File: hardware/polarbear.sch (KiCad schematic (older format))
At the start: 84 parts, among them IC1 ATMEGA32U4, J1 USBMICRO, X1 ATS16B

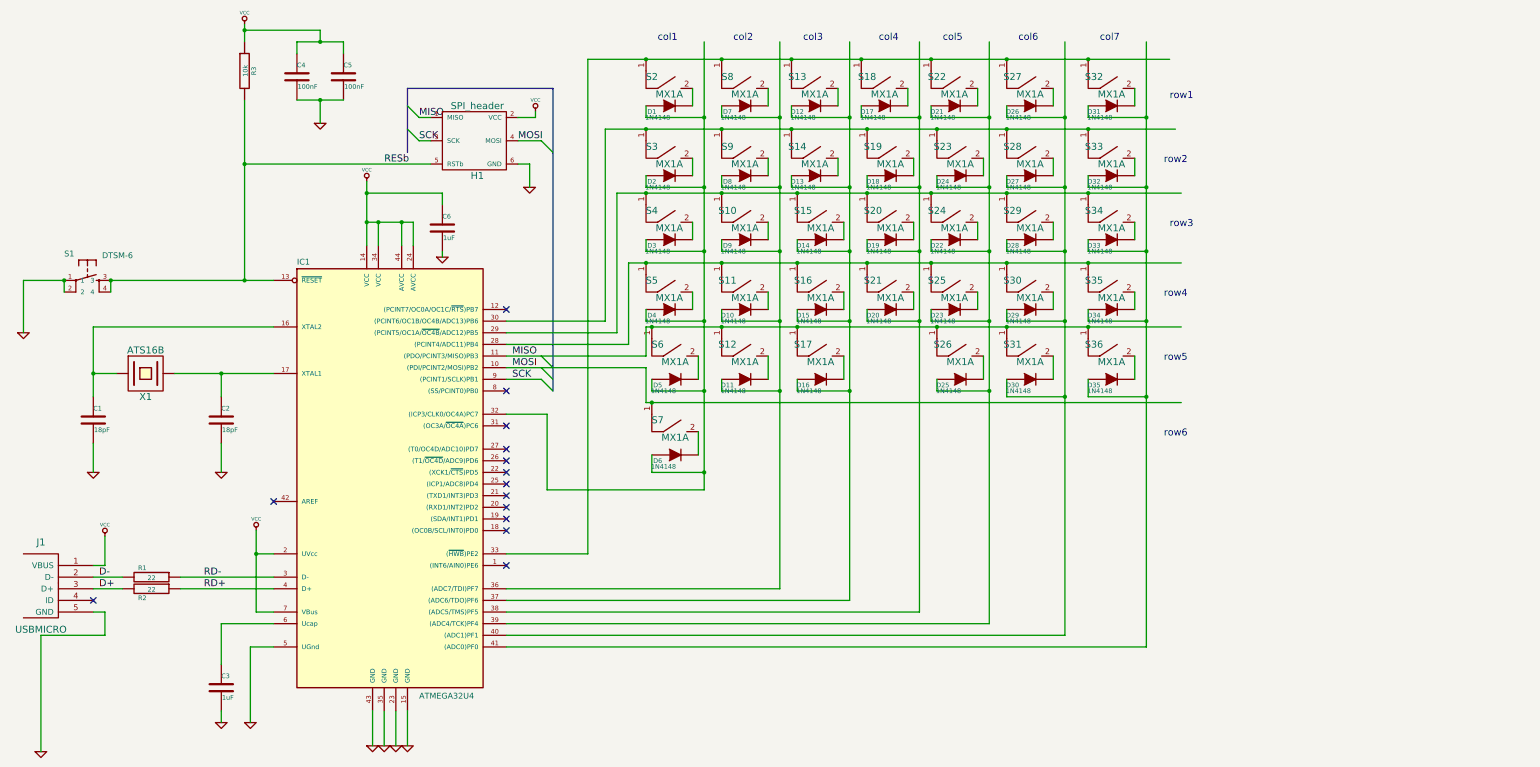
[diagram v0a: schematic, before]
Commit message: Adding support for Tennsy 2.0
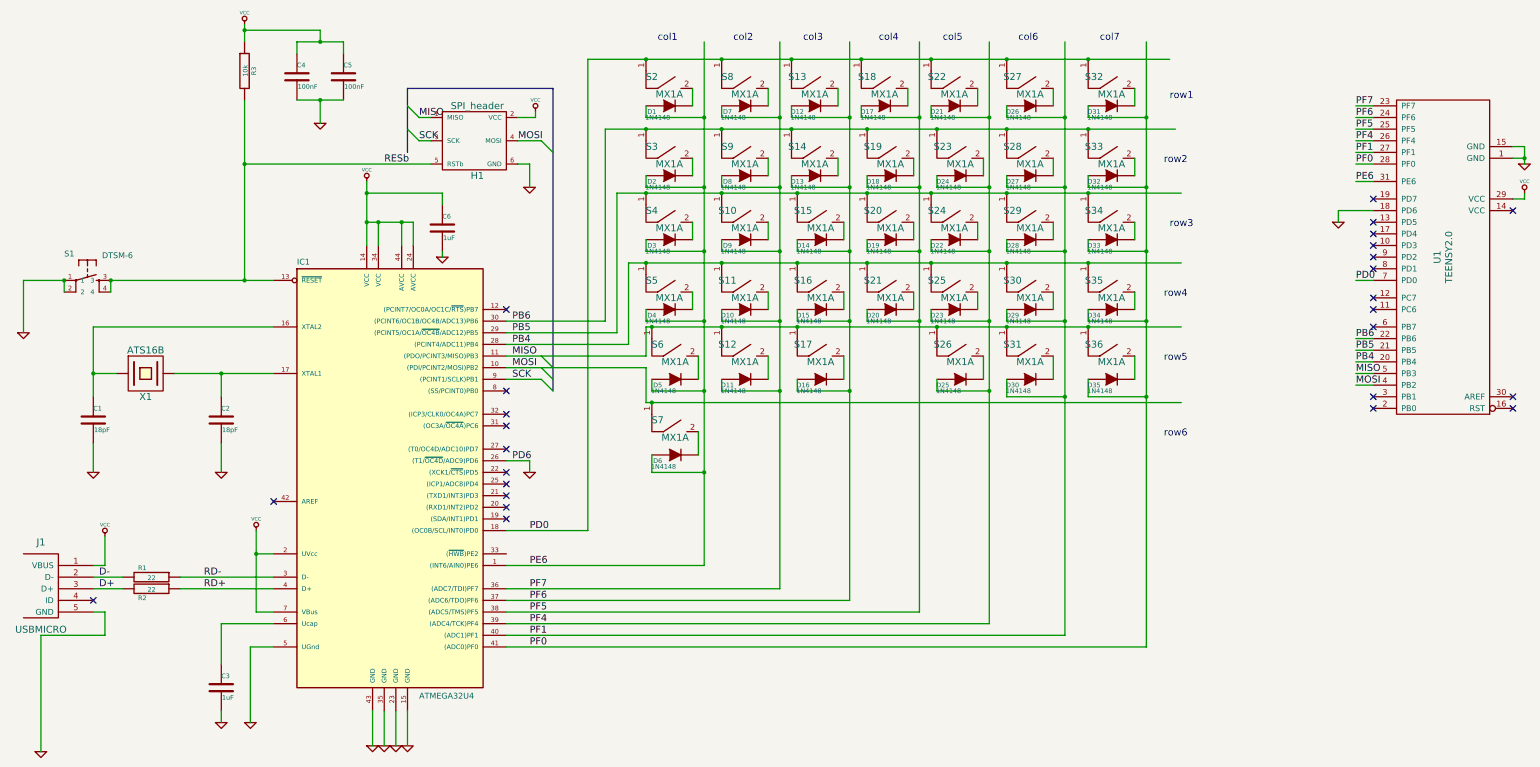
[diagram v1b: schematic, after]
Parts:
- added U1: TEENSY2.0, lib_kicad_mod:TEENSY_2.0, symbol TEENSY2.0
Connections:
- net labels added: PB4, PB5, PB6, PD0, PD6, PE6, PF0, PF1, PF4, PF5, PF6, PF7
- wire segments 199 -> 219
- no-connect marks 14 -> 26

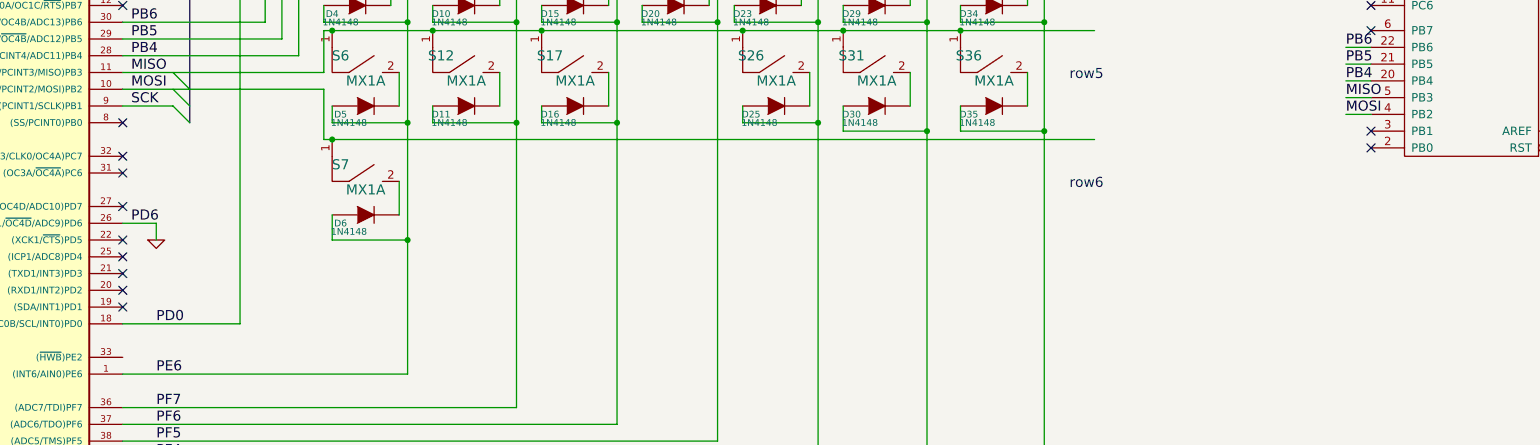
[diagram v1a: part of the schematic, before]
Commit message: Adding WS2128 LED module
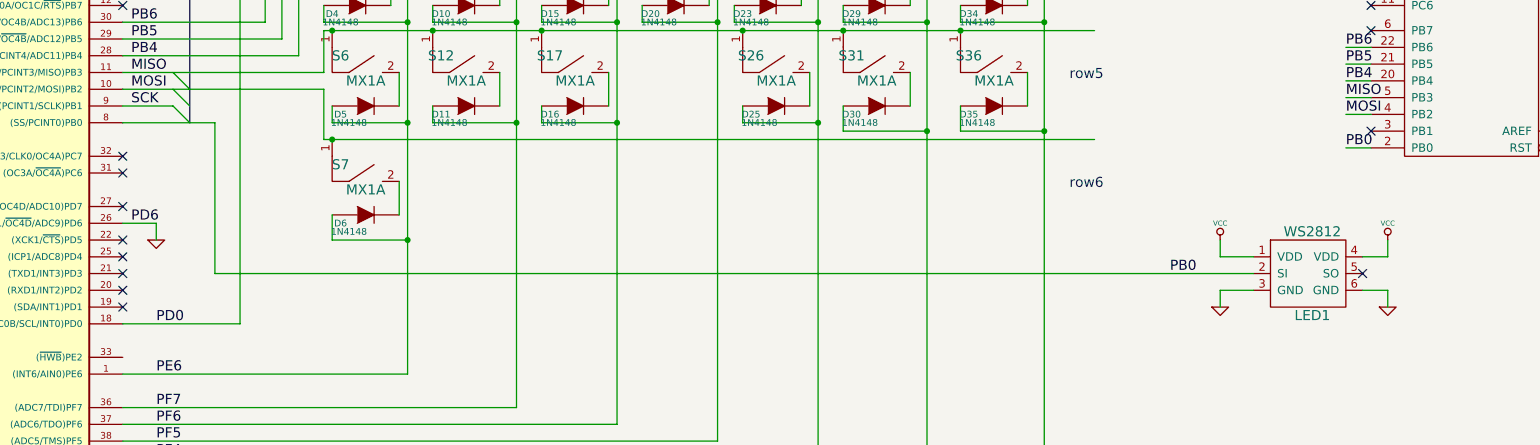
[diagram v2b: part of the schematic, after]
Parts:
- added LED1: WS2812, lib_kicad_mod:WS2128, symbol WS2812
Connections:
- net labels added: PB0
- wire segments 219 -> 231
- no-connect marks 26 -> 25
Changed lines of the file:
@@
 	1    0    0    -1
 $EndComp
-NoConn ~ 5200 4100
 $Comp
 L MX1A S2
@@
 NoConn ~ 12650 3300
 NoConn ~ 12650 3400
-NoConn ~ 12650 4250
 NoConn ~ 12650 3550
 Wire Wire Line
@@
 	13950 2450 13950 2400
 NoConn ~ 12650 4150
+$Comp
+L WS2812 LED1
+U 1 1 57796601
+P 12400 5050
+F 0 "LED1" H 12300 4850 60  0000 C CNN
+F 1 "WS2812" H 12300 5350 60  0000 C CNN
+F 2 "lib_kicad_mod:WS2128" H 12550 5000 60  0001 C CNN
+F 3 "" H 12550 5000 60  0000 C CNN
+	1    12400 5050
+	1    0    0    -1
+$EndComp
+$Comp
+L GND #PWR023
+U 1 1 57797116
+P 11750 5200
+F 0 "#PWR023" H 11750 5200 30  0001 C CNN
+F 1 "GND" H 11750 5130 30  0001 C CNN
+F 2 "" H 11750 5200 60  0000 C CNN
+F 3 "" H 11750 5200 60  0000 C CNN
+	1    11750 5200
+	1    0    0    -1
+$EndComp
+$Comp
+L VCC #PWR024
+U 1 1 57797C0C
+P 11750 4800
+F 0 "#PWR024" H 11750 4900 30  0001 C CNN
+F 1 "VCC" H 11750 4900 30  0000 C CNN
+F 2 "" H 11750 4800 60  0000 C CNN
+F 3 "" H 11750 4800 60  0000 C CNN
+	1    11750 4800
+	1    0    0    -1
+$EndComp
+Wire Wire Line
+	11750 4800 11750 4900
+Wire Wire Line
+	11750 4900 11950 4900
+Wire Wire Line
+	11950 5100 11750 5100
+Wire Wire Line
+	11750 5100 11750 5200
+Wire Wire Line
+	11950 5000 5750 5000
+Wire Wire Line
+	5750 5000 5750 4100
+Wire Wire Line
+	5750 4100 5200 4100
+NoConn ~ 12600 5000
+Text Label 11450 5000 0    60   ~ 0
+PB0
+Text Label 12500 4250 0    60   ~ 0
+PB0
+Wire Wire Line
+	12500 4250 12650 4250
+$Comp
+L VCC #PWR?
+U 1 1 5779BE4D
+P 12750 4800
+F 0 "#PWR?" H 12750 4900 30  0001 C CNN
+F 1 "VCC" H 12750 4900 30  0000 C CNN
+F 2 "" H 12750 4800 60  0000 C CNN
+F 3 "" H 12750 4800 60  0000 C CNN
+	1    12750 4800
+	1    0    0    -1
+$EndComp
+$Comp
+L GND #PWR?
+U 1 1 5779C0BC
+P 12750 5200
+F 0 "#PWR?" H 12750 5200 30  0001 C CNN
+F 1 "GND" H 12750 5130 30  0001 C CNN
+F 2 "" H 12750 5200 60  0000 C CNN
+F 3 "" H 12750 5200 60  0000 C CNN
+	1    12750 5200
+	1    0    0    -1
+$EndComp
+Wire Wire Line
+	12600 4900 12750 4900
+Wire Wire Line
+	12750 4900 12750 4800
+Wire Wire Line
+	12600 5100 12750 5100
+Wire Wire Line
+	12750 5100 12750 5200
 $EndSCHEMATC

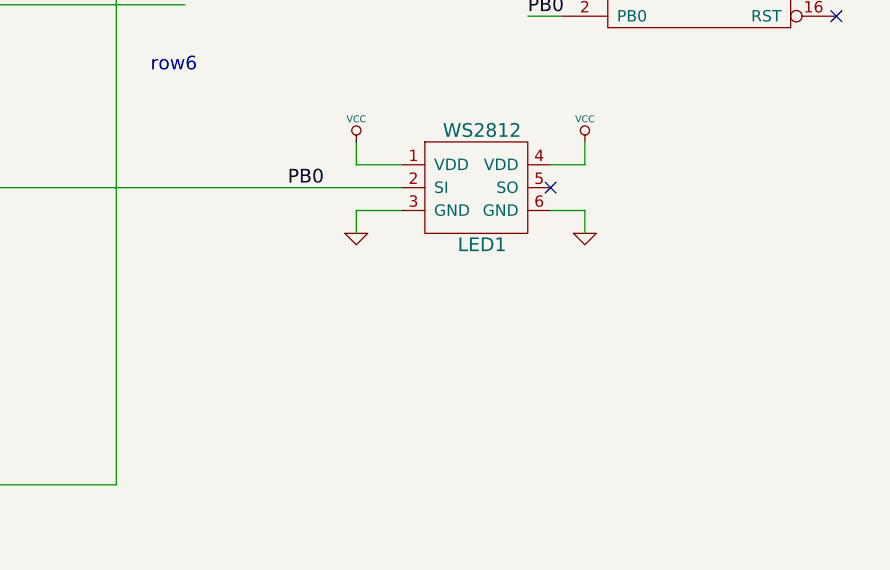
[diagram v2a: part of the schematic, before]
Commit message: Modified design to include 3 WS2128 LED module, added open hardware logo, and re-did routing for VDD/GND.
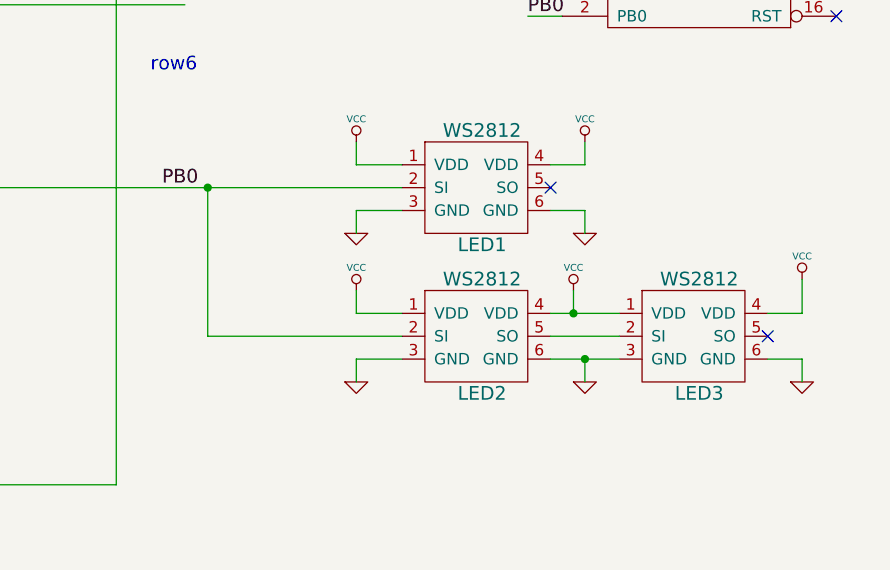
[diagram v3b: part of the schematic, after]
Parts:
- added LED2, LED3: WS2812, lib_kicad_mod:WS2128, symbol WS2812
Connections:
- wire segments 231 -> 246
- no-connect marks 25 -> 26
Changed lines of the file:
@@
 	5750 4100 5200 4100
 NoConn ~ 12600 5000
-Text Label 11450 5000 0    60   ~ 0
-PB0
 Text Label 12500 4250 0    60   ~ 0
 PB0
@@
 	12500 4250 12650 4250
 $Comp
-L VCC #PWR?
+L VCC #PWR025
 U 1 1 5779BE4D
 P 12750 4800
-F 0 "#PWR?" H 12750 4900 30  0001 C CNN
+F 0 "#PWR025" H 12750 4900 30  0001 C CNN
 F 1 "VCC" H 12750 4900 30  0000 C CNN
 F 2 "" H 12750 4800 60  0000 C CNN
@@
 $EndComp
 $Comp
-L GND #PWR?
+L GND #PWR026
 U 1 1 5779C0BC
 P 12750 5200
-F 0 "#PWR?" H 12750 5200 30  0001 C CNN
+F 0 "#PWR026" H 12750 5200 30  0001 C CNN
 F 1 "GND" H 12750 5130 30  0001 C CNN
 F 2 "" H 12750 5200 60  0000 C CNN
@@
 Wire Wire Line
 	12750 5100 12750 5200
+$Comp
+L WS2812 LED2
+U 1 1 57814E9D
+P 12400 5700
+F 0 "LED2" H 12300 5500 60  0000 C CNN
+F 1 "WS2812" H 12300 6000 60  0000 C CNN
+F 2 "lib_kicad_mod:WS2128" H 12550 5650 60  0001 C CNN
+F 3 "" H 12550 5650 60  0000 C CNN
+	1    12400 5700
+	1    0    0    -1
+$EndComp
+$Comp
+L WS2812 LED3
+U 1 1 578154F5
+P 13350 5700
+F 0 "LED3" H 13250 5500 60  0000 C CNN
+F 1 "WS2812" H 13250 6000 60  0000 C CNN
+F 2 "lib_kicad_mod:WS2128" H 13500 5650 60  0001 C CNN
+F 3 "" H 13500 5650 60  0000 C CNN
+	1    13350 5700
+	1    0    0    -1
+$EndComp
+Wire Wire Line
+	12900 5650 12600 5650
+$Comp
+L VCC #PWR027
+U 1 1 57815C08
+P 11750 5450
+F 0 "#PWR027" H 11750 5550 30  0001 C CNN
+F 1 "VCC" H 11750 5550 30  0000 C CNN
+F 2 "" H 11750 5450 60  0000 C CNN
+F 3 "" H 11750 5450 60  0000 C CNN
+	1    11750 5450
+	1    0    0    -1
+$EndComp
+$Comp
+L GND #PWR028
+U 1 1 57815D1B
+P 11750 5850
+F 0 "#PWR028" H 11750 5850 30  0001 C CNN
+F 1 "GND" H 11750 5780 30  0001 C CNN
+F 2 "" H 11750 5850 60  0000 C CNN
+F 3 "" H 11750 5850 60  0000 C CNN
+	1    11750 5850
+	1    0    0    -1
+$EndComp
+Wire Wire Line
+	11100 5000 11100 5650
+Connection ~ 11100 5000
+Wire Wire Line
+	11750 5450 11750 5550
+Wire Wire Line
+	11750 5550 11950 5550
+Wire Wire Line
+	11750 5850 11750 5750
+Wire Wire Line
+	11750 5750 11950 5750
+NoConn ~ 13550 5650
+$Comp
+L VCC #PWR029
+U 1 1 57816473
+P 13700 5400
+F 0 "#PWR029" H 13700 5500 30  0001 C CNN
+F 1 "VCC" H 13700 5500 30  0000 C CNN
+F 2 "" H 13700 5400 60  0000 C CNN
+F 3 "" H 13700 5400 60  0000 C CNN
+	1    13700 5400
+	1    0    0    -1
+$EndComp
+$Comp
+L GND #PWR030
+U 1 1 57816586
+P 13700 5850
+F 0 "#PWR030" H 13700 5850 30  0001 C CNN
+F 1 "GND" H 13700 5780 30  0001 C CNN
+F 2 "" H 13700 5850 60  0000 C CNN
+F 3 "" H 13700 5850 60  0000 C CNN
+	1    13700 5850
+	1    0    0    -1
+$EndComp
+Wire Wire Line
+	13550 5550 13700 5550
+Wire Wire Line
+	13700 5550 13700 5400
+Wire Wire Line
+	13550 5750 13700 5750
+Wire Wire Line
+	13700 5750 13700 5850
+Text Label 10900 5000 0    60   ~ 0
+PB0
+Wire Wire Line
+	11100 5650 11950 5650
+$Comp
+L VCC #PWR?
+U 1 1 57817873
+P 12700 5450
+F 0 "#PWR?" H 12700 5550 30  0001 C CNN
+F 1 "VCC" H 12700 5550 30  0000 C CNN
+F 2 "" H 12700 5450 60  0000 C CNN
+F 3 "" H 12700 5450 60  0000 C CNN
+	1    12700 5450
+	1    0    0    -1
+$EndComp
+$Comp
+L GND #PWR?
+U 1 1 57817986
+P 12750 5850
+F 0 "#PWR?" H 12750 5850 30  0001 C CNN
+F 1 "GND" H 12750 5780 30  0001 C CNN
+F 2 "" H 12750 5850 60  0000 C CNN
+F 3 "" H 12750 5850 60  0000 C CNN
+	1    12750 5850
+	1    0    0    -1
+$EndComp
+Wire Wire Line
+	12600 5550 12900 5550
+Wire Wire Line
+	12700 5550 12700 5450
+Connection ~ 12700 5550
+Wire Wire Line
+	12600 5750 12900 5750
+Wire Wire Line
+	12750 5750 12750 5850
+Connection ~ 12750 5750
 $EndSCHEMATC
